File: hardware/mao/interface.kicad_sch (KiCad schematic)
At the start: 24 parts, among them J301 LCD, Q302 DMG2302UK, SW301 SKQGADE010, U301 DRV5012AEDMRR, U302 DRV5012AEDMRR, U304 TLV9061IDBVR

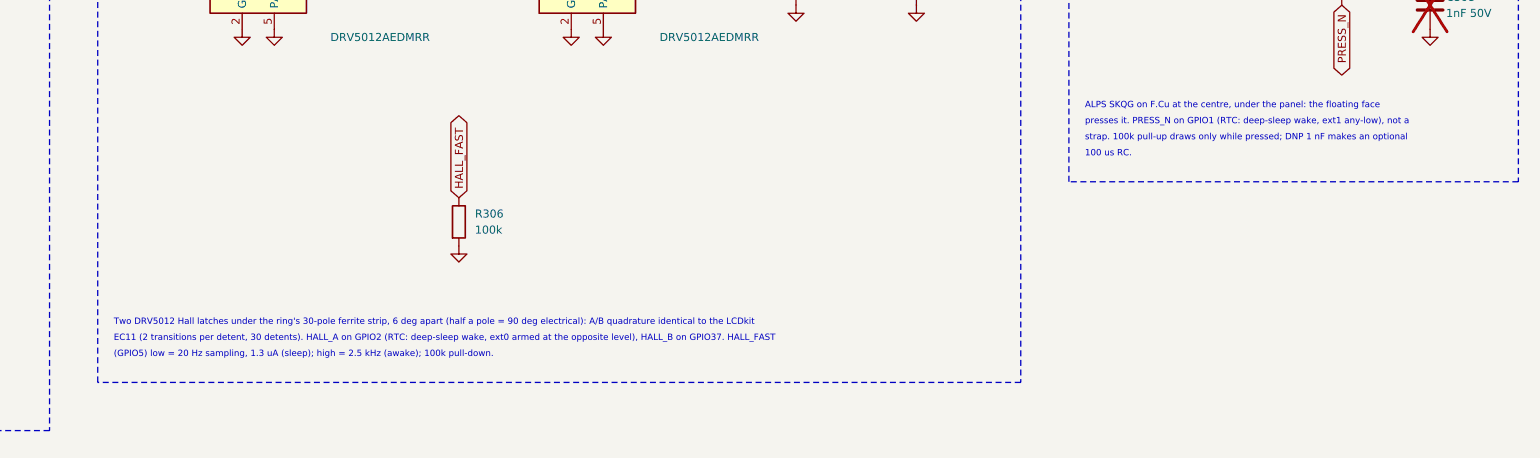
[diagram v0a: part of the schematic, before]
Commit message: A1 capture/layout follow the pin swaps (ERC 0); escapes and fixture pads moved with their nets
Co-Authored-By: Claude Opus 5.5 <noreply@anthropic.com>
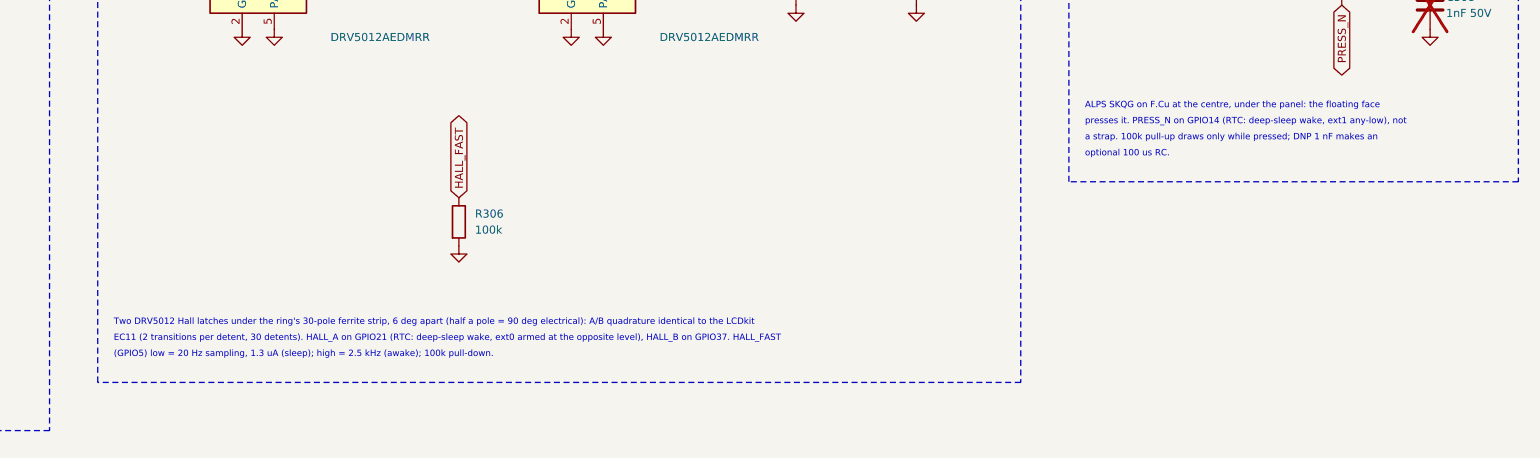
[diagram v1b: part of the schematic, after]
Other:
- note added: "EC11 (2 transitions per detent, 30 detents). HALL_A on GPIO21 (RTC: deep-sleep wake, ext0 armed at the opposite level), HALL_B on GPIO37. HALL_FAST"
- note added: "a strap. 100k pull-up draws only while pressed; DNP 1 nF makes an"
- note added: "optional 100 us RC."
- note added: "presses it. PRESS_N on GPIO14 (RTC: deep-sleep wake, ext1 any-low), not"
- note removed: "100 us RC."
- note removed: "EC11 (2 transitions per detent, 30 detents). HALL_A on GPIO2 (RTC: deep-sleep wake, ext0 armed at the opposite level), HALL_B on GPIO37. HALL_FAST"
- note removed: "presses it. PRESS_N on GPIO1 (RTC: deep-sleep wake, ext1 any-low), not a"
- note removed: "strap. 100k pull-up draws only while pressed; DNP 1 nF makes an optional"
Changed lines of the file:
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@@
 		)
 	)
-	(text "EC11 (2 transitions per detent, 30 detents). HALL_A on GPIO2 (RTC: deep-sleep wake, ext0 armed at the opposite level), HALL_B on GPIO37. HALL_FAST"
+	(text "EC11 (2 transitions per detent, 30 detents). HALL_A on GPIO21 (RTC: deep-sleep wake, ext0 armed at the opposite level), HALL_B on GPIO37. HALL_FAST"
 		(exclude_from_sim no)
 		(at 121.92 96.52 0)
@@
 		)
 	)
-	(text "presses it. PRESS_N on GPIO1 (RTC: deep-sleep wake, ext1 any-low), not a"
+	(text "presses it. PRESS_N on GPIO14 (RTC: deep-sleep wake, ext1 any-low), not"
 		(exclude_from_sim no)
 		(at 275.59 62.23 0)
@@
 		)
 	)
-	(text "strap. 100k pull-up draws only while pressed; DNP 1 nF makes an optional"
+	(text "a strap. 100k pull-up draws only while pressed; DNP 1 nF makes an"
 		(exclude_from_sim no)
 		(at 275.59 64.77 0)
@@
 		)
 	)
-	(text "100 us RC."
+	(text "optional 100 us RC."
 		(exclude_from_sim no)
 		(at 275.59 67.31 0)

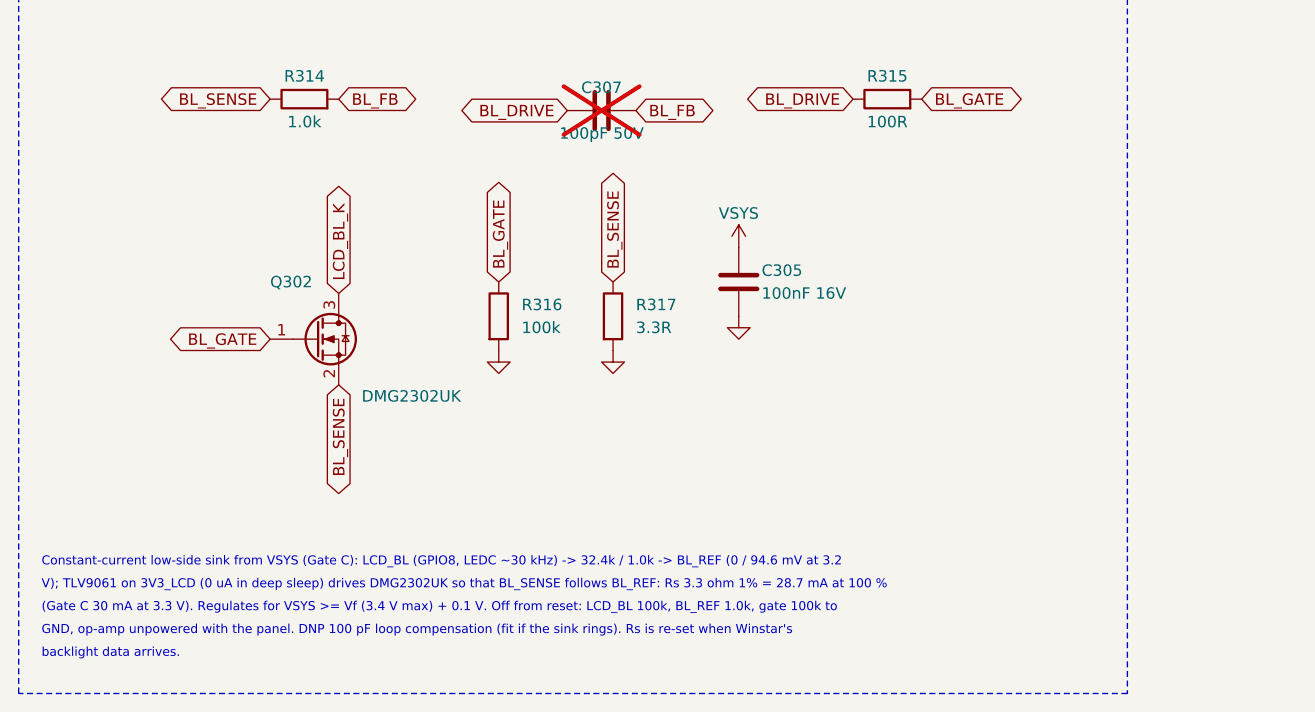
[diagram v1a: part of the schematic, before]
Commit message: A1 BOM (design review 2026-10-06): charger IN/BAT 2.2 uF 25 V 0402, DRV2605LDGST, DMG2302UKQ-7; backlight reference 95.8 mV -> 29.0 mA
C101/C103 move from 1 uF to 2.2 uF 25 V 0402 (CL05A225KA5NUNC, C307418) so at least 1 uF remains under DC bias
(TI SLUSF65B 7.2.2.3). DRV2605LDGSR -> DRV2605LDGST (C425927, same part, 250 reel) and DMG2302UK-7 -> DMG2302UKQ-7
(C5224573, same pinout) for stock. Fixes the backlight arithmetic in the capture notes (N7).

Co-Authored-By: Claude Opus 5.5 <noreply@anthropic.com>
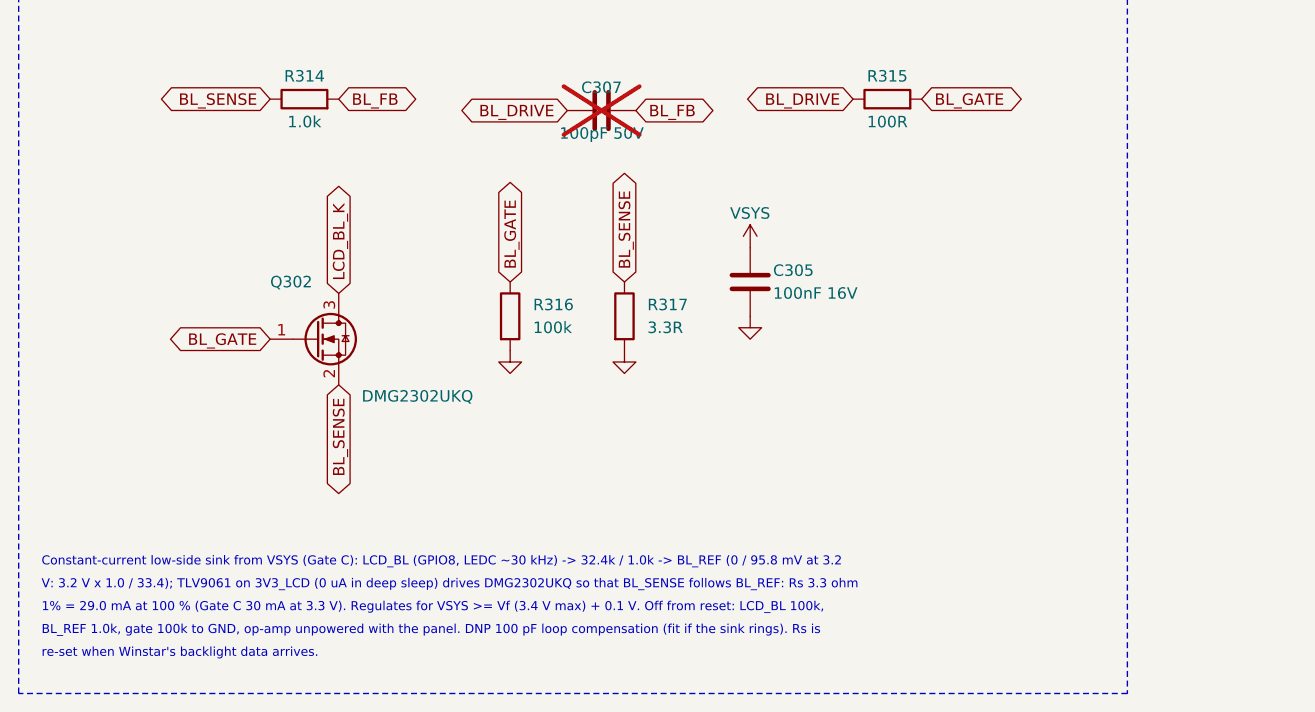
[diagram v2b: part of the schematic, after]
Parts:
- Q302: value DMG2302UK -> DMG2302UKQ; LCSC C460977 -> C5224573; MPN DMG2302UK-7 -> DMG2302UKQ-7
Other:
- note added: "1% = 29.0 mA at 100 % (Gate C 30 mA at 3.3 V). Regulates for VSYS >= Vf (3.4 V max) + 0.1 V. Off from reset: LCD_BL 100k,"
- note added: "BL_REF 1.0k, gate 100k to GND, op-amp unpowered with the panel. DNP 100 pF loop compensation (fit if the sink rings). Rs is"
- note added: "Constant-current low-side sink from VSYS (Gate C): LCD_BL (GPIO8, LEDC ~30 kHz) -> 32.4k / 1.0k -> BL_REF (0 / 95.8 mV at 3.2"
- note added: "V: 3.2 V x 1.0 / 33.4); TLV9061 on 3V3_LCD (0 uA in deep sleep) drives DMG2302UKQ so that BL_SENSE follows BL_REF: Rs 3.3 ohm"
- note added: "re-set when Winstar's backlight data arrives."
- note removed: "(Gate C 30 mA at 3.3 V). Regulates for VSYS >= Vf (3.4 V max) + 0.1 V. Off from reset: LCD_BL 100k, BL_REF 1.0k, gate 100k to"
- note removed: "Constant-current low-side sink from VSYS (Gate C): LCD_BL (GPIO8, LEDC ~30 kHz) -> 32.4k / 1.0k -> BL_REF (0 / 94.6 mV at 3.2"
- note removed: "GND, op-amp unpowered with the panel. DNP 100 pF loop compensation (fit if the sink rings). Rs is re-set when Winstar's"
- note removed: "V); TLV9061 on 3V3_LCD (0 uA in deep sleep) drives DMG2302UK so that BL_SENSE follows BL_REF: Rs 3.3 ohm 1% = 28.7 mA at 100 %"
- note removed: "backlight data arrives."
- moved on the sheet: C305, R316, R317
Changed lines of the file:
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@@
 		)
 	)
-	(text "Constant-current low-side sink from VSYS (Gate C): LCD_BL (GPIO8, LEDC ~30 kHz) -> 32.4k / 1.0k -> BL_REF (0 / 94.6 mV at 3.2"
+	(text "Constant-current low-side sink from VSYS (Gate C): LCD_BL (GPIO8, LEDC ~30 kHz) -> 32.4k / 1.0k -> BL_REF (0 / 95.8 mV at 3.2"
 		(exclude_from_sim no)
 		(at 15.24 219.71 0)
@@
 		)
 	)
-	(text "V); TLV9061 on 3V3_LCD (0 uA in deep sleep) drives DMG2302UK so that BL_SENSE follows BL_REF: Rs 3.3 ohm 1% = 28.7 mA at 100 %"
+	(text "V: 3.2 V x 1.0 / 33.4); TLV9061 on 3V3_LCD (0 uA in deep sleep) drives DMG2302UKQ so that BL_SENSE follows BL_REF: Rs 3.3 ohm"
 		(exclude_from_sim no)
 		(at 15.24 222.25 0)
@@
 		)
 	)
-	(text "(Gate C 30 mA at 3.3 V). Regulates for VSYS >= Vf (3.4 V max) + 0.1 V. Off from reset: LCD_BL 100k, BL_REF 1.0k, gate 100k to"
+	(text "1% = 29.0 mA at 100 % (Gate C 30 mA at 3.3 V). Regulates for VSYS >= Vf (3.4 V max) + 0.1 V. Off from reset: LCD_BL 100k,"
 		(exclude_from_sim no)
 		(at 15.24 224.79 0)
@@
 		)
 	)
-	(text "GND, op-amp unpowered with the panel. DNP 100 pF loop compensation (fit if the sink rings). Rs is re-set when Winstar's"
+	(text "BL_REF 1.0k, gate 100k to GND, op-amp unpowered with the panel. DNP 100 pF loop compensation (fit if the sink rings). Rs is"
 		(exclude_from_sim no)
 		(at 15.24 227.33 0)
@@
 		)
 	)
-	(text "backlight data arrives."
+	(text "re-set when Winstar's backlight data arrives."
 		(exclude_from_sim no)
 		(at 15.24 229.87 0)
@@
 			)
 		)
-		(property "Description" "reference divider top: 3.2 V -> 94.6 mV"
+		(property "Description" "reference divider top: 3.2 V x 1.0 / 33.4 = 95.8 mV"
 			(at 43.18 129.54 0)
 			(effects
@@
 			)
 		)
-		(property "Value" "DMG2302UK"
+		(property "Value" "DMG2302UKQ"
 			(at 50.8 200.66 0)
 			(effects
@@
 			)
 		)
-		(property "Description" "backlight sink FET (pins 1 G, 2 S, 3 D)"
+		(property "Description" "backlight sink FET (pins 1 G, 2 S, 3 D); DMG2302UKQ-7 = the automotive-qualified DMG2302UK, same pinout"
 			(at 45.72 194.31 0)
 			(effects
@@
 			)
 		)
-		(property "MPN" "DMG2302UK-7"
+		(property "MPN" "DMG2302UKQ-7"
 			(at 45.72 194.31 0)
 			(effects
@@
 			)
 		)
-		(property "LCSC" "C460977"
+		(property "LCSC" "C5224573"
 			(at 45.72 194.31 0)
 			(effects
@@
 	(symbol
 		(lib_id "Device:R")
-		(at 66.04 191.77 0)
+		(at 67.31 191.77 0)
 		(unit 1)
 		(exclude_from_sim no)
@@
 		(fields_autoplaced yes)
 		(property "Reference" "R316"
-			(at 68.58 190.5 0)
+			(at 69.85 190.5 0)
 			(effects
 				(font (size 1.27 1.27))
@@
 		)
 		(property "Value" "100k"
-			(at 68.58 193.04 0)
+			(at 69.85 193.04 0)
 			(effects
 				(font (size 1.27 1.27))
@@
 		)
 		(property "Footprint" "Resistor_SMD:R_0402_1005Metric"
-			(at 66.04 191.77 0)
-			(effects
-				(font (size 1.27 1.27))
-				(hide yes)
-			)
-		)
-		(property "Datasheet" ""
-			(at 66.04 191.77 0)
+			(at 67.31 191.77 0)
+			(effects
+				(font (size 1.27 1.27))
+				(hide yes)
+			)
+		)
+		(property "Datasheet" ""
+			(at 67.31 191.77 0)
 			(effects
 				(font (size 1.27 1.27))
@@
 		)
 		(property "Description" "gate held off with the op-amp unpowered"
-			(at 66.04 191.77 0)
+			(at 67.31 191.77 0)
 			(effects
 				(font (size 1.27 1.27))
@@
 		)
 		(property "MPN" "0402WGF1003TCE"
-			(at 66.04 191.77 0)
+			(at 67.31 191.77 0)
 			(effects
 				(font (size 1.27 1.27))
@@
 		)
 		(property "Manufacturer" "UNI-ROYAL"
-			(at 66.04 191.77 0)
+			(at 67.31 191.77 0)
 			(effects
 				(font (size 1.27 1.27))
@@
 		)
 		(property "LCSC" "C25741"
-			(at 66.04 191.77 0)
+			(at 67.31 191.77 0)
 			(effects
 				(font (size 1.27 1.27))
@@
 	(global_label "BL_GATE"
 		(shape bidirectional)
-		(at 66.04 187.96 90)
+		(at 67.31 187.96 90)
 		(fields_autoplaced yes)
 		(effects
@@
 	(symbol
 		(lib_id "power:GND")
-		(at 66.04 195.58 0)
+		(at 67.31 195.58 0)
 		(unit 1)
 		(exclude_from_sim no)
@@
 		(dnp no)
 		(property "Reference" "#PWR429"
-			(at 66.04 195.58 0)
+			(at 67.31 195.58 0)
 			(effects
 				(font (size 1.27 1.27))
@@
 		)
 		(property "Value" "GND"
-			(at 66.04 199.39 0)
+			(at 67.31 199.39 0)
 			(effects
 				(font (size 1.27 1.27))
@@
 		)
 		(property "Footprint" ""
-			(at 66.04 195.58 0)
-			(effects
-				(font (size 1.27 1.27))
-				(hide yes)
-			)
-		)
-		(property "Datasheet" ""
-			(at 66.04 195.58 0)
+			(at 67.31 195.58 0)
+			(effects
+				(font (size 1.27 1.27))
+				(hide yes)
+			)
+		)
+		(property "Datasheet" ""
+			(at 67.31 195.58 0)
 			(effects
 				(font (size 1.27 1.27))
@@
 	(symbol
 		(lib_id "Device:R")
-		(at 78.74 191.77 0)
+		(at 80.01 191.77 0)
 		(unit 1)
 		(exclude_from_sim no)
@@
 		(fields_autoplaced yes)
 		(property "Reference" "R317"
-			(at 81.28 190.5 0)
+			(at 82.55 190.5 0)
 			(effects
 				(font (size 1.27 1.27))
@@
 		)
 		(property "Value" "3.3R"
-			(at 81.28 193.04 0)
+			(at 82.55 193.04 0)
 			(effects
 				(font (size 1.27 1.27))
@@
 		)
 		(property "Footprint" "Resistor_SMD:R_0603_1608Metric"
-			(at 78.74 191.77 0)
-			(effects
-				(font (size 1.27 1.27))
-				(hide yes)
-			)
-		)
-		(property "Datasheet" ""
-			(at 78.74 191.77 0)
-			(effects
-				(font (size 1.27 1.27))
-				(hide yes)
-			)
-		)
-		(property "Description" "Rs: 94.6 mV / 3.3 ohm = 28.7 mA LED current"
-			(at 78.74 191.77 0)
+			(at 80.01 191.77 0)
+			(effects
+				(font (size 1.27 1.27))
+				(hide yes)
+			)
+		)
+		(property "Datasheet" ""
+			(at 80.01 191.77 0)
+			(effects
+				(font (size 1.27 1.27))
+				(hide yes)
+			)
+		)
+		(property "Description" "Rs: 95.8 mV / 3.3 ohm = 29.0 mA LED current"
+			(at 80.01 191.77 0)
 			(effects
 				(font (size 1.27 1.27))
@@
 		)
 		(property "MPN" "0603WAF330KT5E"
-			(at 78.74 191.77 0)
+			(at 80.01 191.77 0)
 			(effects
 				(font (size 1.27 1.27))
@@
 		)
 		(property "Manufacturer" "UNI-ROYAL"
-			(at 78.74 191.77 0)
+			(at 80.01 191.77 0)
 			(effects
 				(font (size 1.27 1.27))
@@
 		)
 		(property "LCSC" "C22979"
-			(at 78.74 191.77 0)
+			(at 80.01 191.77 0)
 			(effects
 				(font (size 1.27 1.27))
@@
 	(global_label "BL_SENSE"
 		(shape bidirectional)
-		(at 78.74 187.96 90)
+		(at 80.01 187.96 90)
 		(fields_autoplaced yes)
 		(effects
@@
 	(symbol
 		(lib_id "power:GND")
-		(at 78.74 195.58 0)
+		(at 80.01 195.58 0)
 		(unit 1)
 		(exclude_from_sim no)
@@
 		(dnp no)
 		(property "Reference" "#PWR430"
-			(at 78.74 195.58 0)
+			(at 80.01 195.58 0)
 			(effects
 				(font (size 1.27 1.27))
@@
 		)
 		(property "Value" "GND"
-			(at 78.74 199.39 0)
+			(at 80.01 199.39 0)
 			(effects
 				(font (size 1.27 1.27))
@@
 		)
 		(property "Footprint" ""
-			(at 78.74 195.58 0)
-			(effects
-				(font (size 1.27 1.27))
-				(hide yes)
-			)
-		)
-		(property "Datasheet" ""
-			(at 78.74 195.58 0)
+			(at 80.01 195.58 0)
+			(effects
+				(font (size 1.27 1.27))
+				(hide yes)
+			)
+		)
+		(property "Datasheet" ""
+			(at 80.01 195.58 0)
 			(effects
 				(font (size 1.27 1.27))
@@
 	(symbol
 		(lib_id "Device:C")
-		(at 92.71 187.96 0)
+		(at 93.98 187.96 0)
 		(unit 1)
 		(exclude_from_sim no)
@@
 		(fields_autoplaced yes)
 		(property "Reference" "C305"
-			(at 95.25 186.69 0)
+			(at 96.52 186.69 0)
 			(effects
 				(font (size 1.27 1.27))
@@
 		)
 		(property "Value" "100nF 16V"
-			(at 95.25 189.23 0)
+			(at 96.52 189.23 0)
 			(effects
 				(font (size 1.27 1.27))
@@
 		)
 		(property "Footprint" "Capacitor_SMD:C_0402_1005Metric"
-			(at 92.71 187.96 0)
-			(effects
-				(font (size 1.27 1.27))
-				(hide yes)
-			)
-		)
-		(property "Datasheet" ""
-			(at 92.71 187.96 0)
+			(at 93.98 187.96 0)
+			(effects
+				(font (size 1.27 1.27))
+				(hide yes)
+			)
+		)
+		(property "Datasheet" ""
+			(at 93.98 187.96 0)
 			(effects
 				(font (size 1.27 1.27))
@@
 		)
 		(property "Description" "VLED+ bypass at J301 pin 7"
-			(at 92.71 187.96 0)
+			(at 93.98 187.96 0)
 			(effects
 				(font (size 1.27 1.27))
@@
 		)
 		(property "MPN" "CL05B104KO5NNNC"
-			(at 92.71 187.96 0)
+			(at 93.98 187.96 0)
 			(effects
 				(font (size 1.27 1.27))
@@
 		)
 		(property "Manufacturer" "Samsung"
-			(at 92.71 187.96 0)
+			(at 93.98 187.96 0)
 			(effects
 				(font (size 1.27 1.27))
@@
 		)
 		(property "LCSC" "C1525"
-			(at 92.71 187.96 0)
+			(at 93.98 187.96 0)
 			(effects
 				(font (size 1.27 1.27))
@@
 	(symbol
 		(lib_id "MAO:VSYS")
-		(at 92.71 184.15 0)
+		(at 93.98 184.15 0)
 		(unit 1)
 		(exclude_from_sim no)
@@
 		(dnp no)
 		(property "Reference" "#PWR431"
-			(at 92.71 184.15 0)
+			(at 93.98 184.15 0)
 			(effects
 				(font (size 1.27 1.27))
@@
 		)
 		(property "Value" "VSYS"
-			(at 92.71 180.34 0)
+			(at 93.98 180.34 0)
 			(effects
 				(font (size 1.27 1.27))
@@
 		)
 		(property "Footprint" ""
-			(at 92.71 184.15 0)
-			(effects
-				(font (size 1.27 1.27))
-				(hide yes)
-			)
-		)
-		(property "Datasheet" ""
-			(at 92.71 184.15 0)
+			(at 93.98 184.15 0)
+			(effects
+				(font (size 1.27 1.27))
+				(hide yes)
+			)
+		)
+		(property "Datasheet" ""
+			(at 93.98 184.15 0)
 			(effects
 				(font (size 1.27 1.27))
@@
 	(symbol
 		(lib_id "power:GND")
-		(at 92.71 191.77 0)
+		(at 93.98 191.77 0)
 		(unit 1)
 		(exclude_from_sim no)
@@
 		(dnp no)
 		(property "Reference" "#PWR432"
-			(at 92.71 191.77 0)
+			(at 93.98 191.77 0)
 			(effects
 				(font (size 1.27 1.27))
@@
 		)
 		(property "Value" "GND"
-			(at 92.71 195.58 0)
+			(at 93.98 195.58 0)
 			(effects
 				(font (size 1.27 1.27))
@@
 		)
 		(property "Footprint" ""
-			(at 92.71 191.77 0)
-			(effects
-				(font (size 1.27 1.27))
-				(hide yes)
-			)
-		)
-		(property "Datasheet" ""
-			(at 92.71 191.77 0)
-			(effects
-				(font (size 1.27 1.27))
+			(at 93.98 191.77 0)
+			(effects
+				(font (size 1.27 1.27))
+				(hide yes)
+			)
+		)
+		(property "Datasheet" ""
+			(at 93.98 191.77 0)
+			(effects
+				(font (size 1.27 1.27))
